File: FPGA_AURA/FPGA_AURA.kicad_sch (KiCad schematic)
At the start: 0 parts

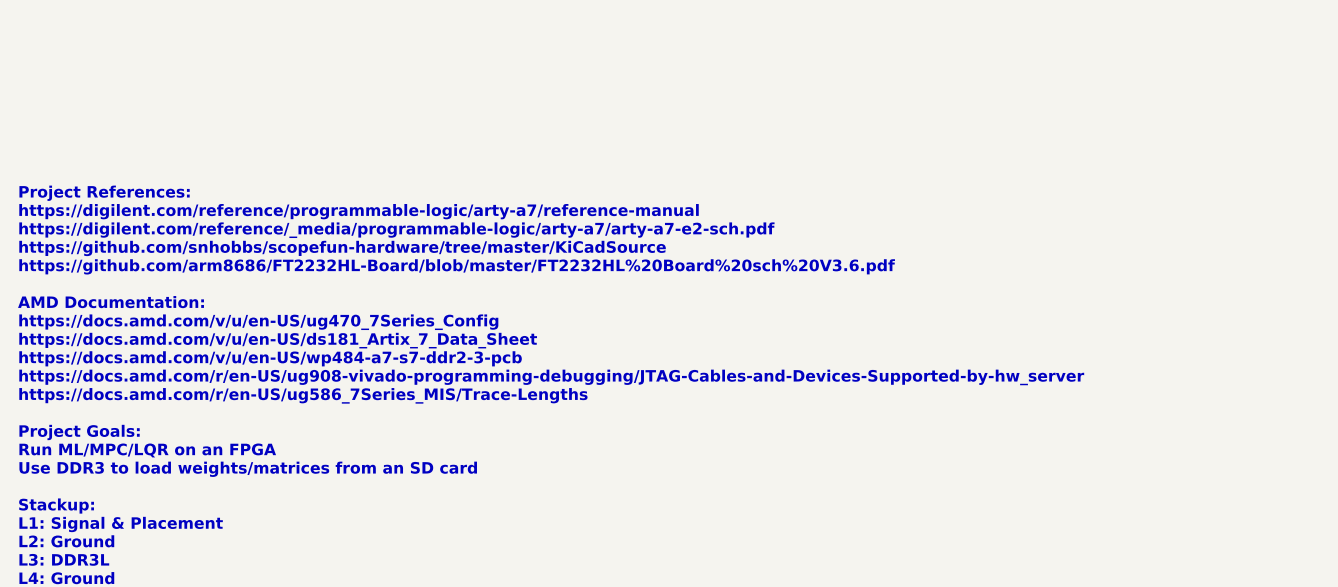
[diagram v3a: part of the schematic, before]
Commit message: Time domain tuning setup.
The tuning profiles and net classes have been setup to enable time domain tuning.
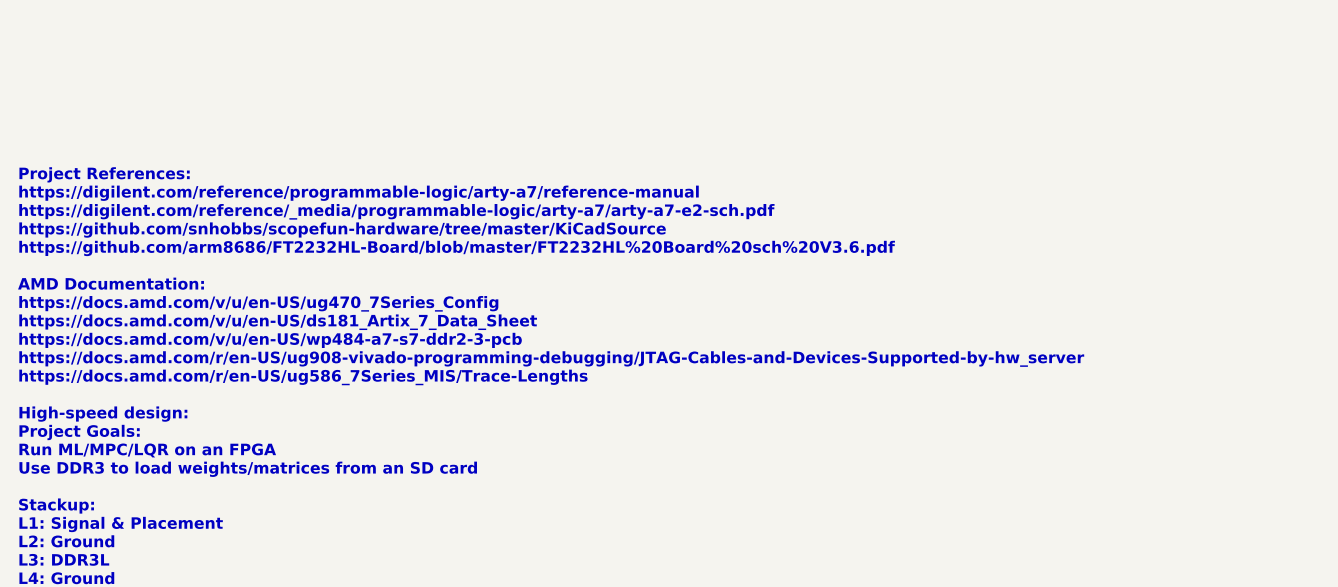
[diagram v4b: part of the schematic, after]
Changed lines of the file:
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@@
 		(company "Alexander Armitage")
 	)
-	(text "Project References:\nhttps://digilent.com/reference/programmable-logic/arty-a7/reference-manual\nhttps://digilent.com/reference/_media/programmable-logic/arty-a7/arty-a7-e2-sch.pdf\nhttps://github.com/snhobbs/scopefun-hardware/tree/master/KiCadSource\nhttps://github.com/arm8686/FT2232HL-Board/blob/master/FT2232HL%20Board%20sch%20V3.6.pdf\n\nAMD Documentation:\nhttps://docs.amd.com/v/u/en-US/ug470_7Series_Config\nhttps://docs.amd.com/v/u/en-US/ds181_Artix_7_Data_Sheet\nhttps://docs.amd.com/v/u/en-US/wp484-a7-s7-ddr2-3-pcb\nhttps://docs.amd.com/r/en-US/ug908-vivado-programming-debugging/JTAG-Cables-and-Devices-Supported-by-hw_server\nhttps://docs.amd.com/r/en-US/ug586_7Series_MIS/Trace-Lengths\n\nProject Goals:\nRun ML/MPC/LQR on an FPGA\nUse DDR3 to load weights/matrices from an SD card\n\nStackup:\nL1: Signal & Placement\nL2: Ground\nL3: DDR3L\nL4: Ground\nL5: DDR3L\nL6: Ground\nL7: Power\nL8: Signal & Placement\n\nDDR Routing:\nAccording to WP484, route single ended as 50ohm, diff as 100ohm\nChose closest ODT to 50ohm"
+	(text "Project References:\nhttps://digilent.com/reference/programmable-logic/arty-a7/reference-manual\nhttps://digilent.com/reference/_media/programmable-logic/arty-a7/arty-a7-e2-sch.pdf\nhttps://github.com/snhobbs/scopefun-hardware/tree/master/KiCadSource\nhttps://github.com/arm8686/FT2232HL-Board/blob/master/FT2232HL%20Board%20sch%20V3.6.pdf\n\nAMD Documentation:\nhttps://docs.amd.com/v/u/en-US/ug470_7Series_Config\nhttps://docs.amd.com/v/u/en-US/ds181_Artix_7_Data_Sheet\nhttps://docs.amd.com/v/u/en-US/wp484-a7-s7-ddr2-3-pcb\nhttps://docs.amd.com/r/en-US/ug908-vivado-programming-debugging/JTAG-Cables-and-Devices-Supported-by-hw_server\nhttps://docs.amd.com/r/en-US/ug586_7Series_MIS/Trace-Lengths\n\nHigh-speed design:\nProject Goals:\nRun ML/MPC/LQR on an FPGA\nUse DDR3 to load weights/matrices from an SD card\n\nStackup:\nL1: Signal & Placement\nL2: Ground\nL3: DDR3L\nL4: Ground\nL5: DDR3L\nL6: Ground\nL7: Power\nL8: Signal & Placement\n\nDDR Routing:\nAccording to WP484, route single ended as 50ohm, diff as 100ohm\nChose closest ODT to 50ohm"
 		(exclude_from_sim no)
 		(at 25.4 190.5 0)

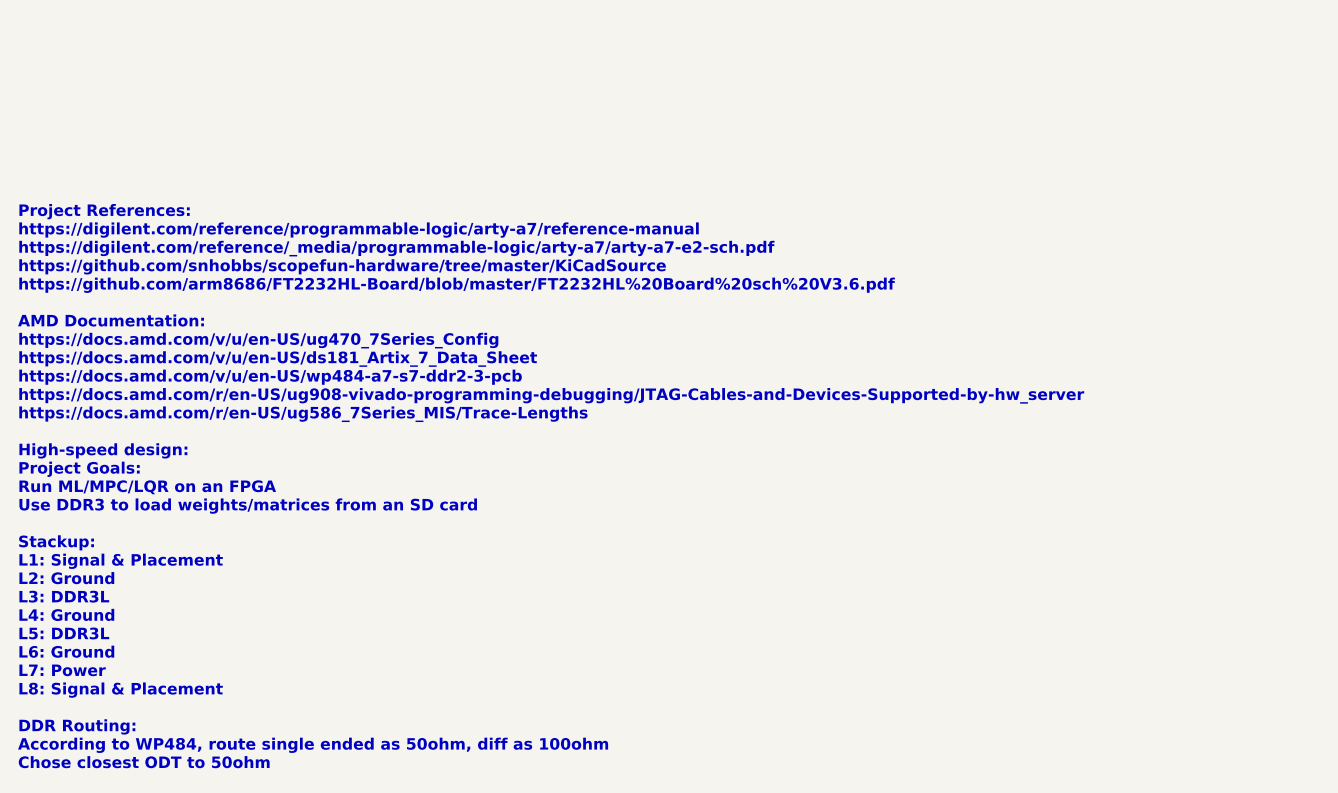
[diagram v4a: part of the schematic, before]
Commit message: Changing stackup to 10 layers and connectors change
Development has been slow due to SI concerns with 8 layers so changing the layer count to 10 will simplify design. The picoblade/SD connector(s) are large and not high speed, so a high speed mezzanine will be used to go to a daughter board with the picoblade connectors and SD card, or other devices/protocols e.g. ADCs, COAX, IMUs, etc.
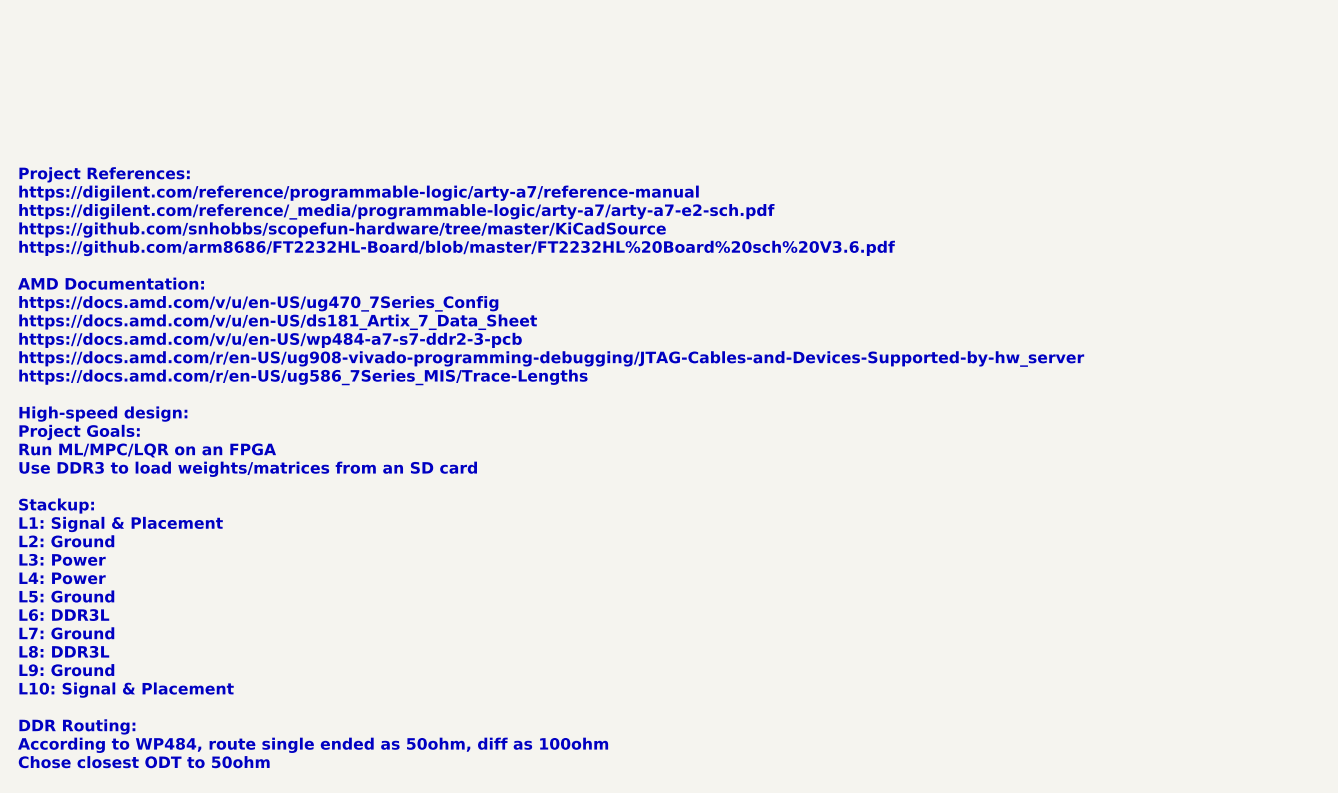
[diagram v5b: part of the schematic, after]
